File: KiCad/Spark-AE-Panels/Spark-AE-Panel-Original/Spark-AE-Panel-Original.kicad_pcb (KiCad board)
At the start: 4 copper layers, 50 x 101 mm, 1 part

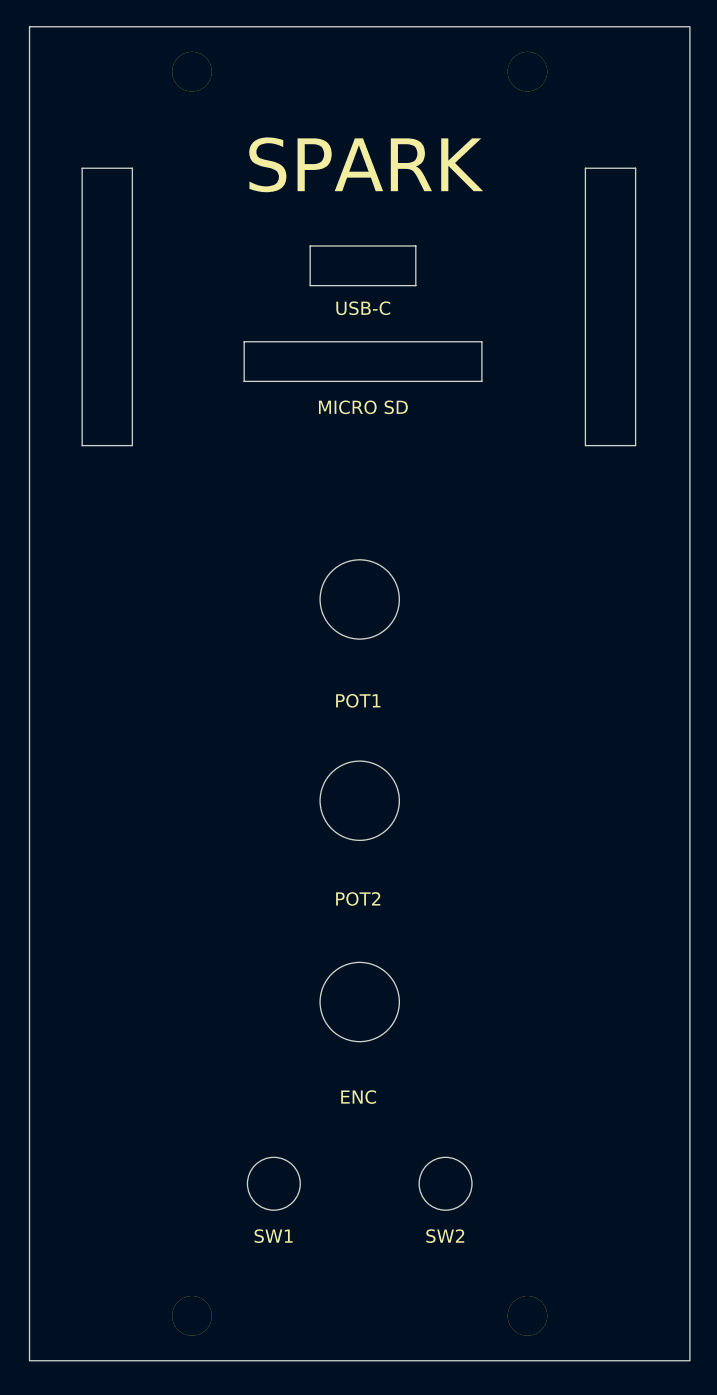
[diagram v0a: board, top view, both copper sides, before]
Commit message: rough pass over original mk0.1 panel. needs confirmation.
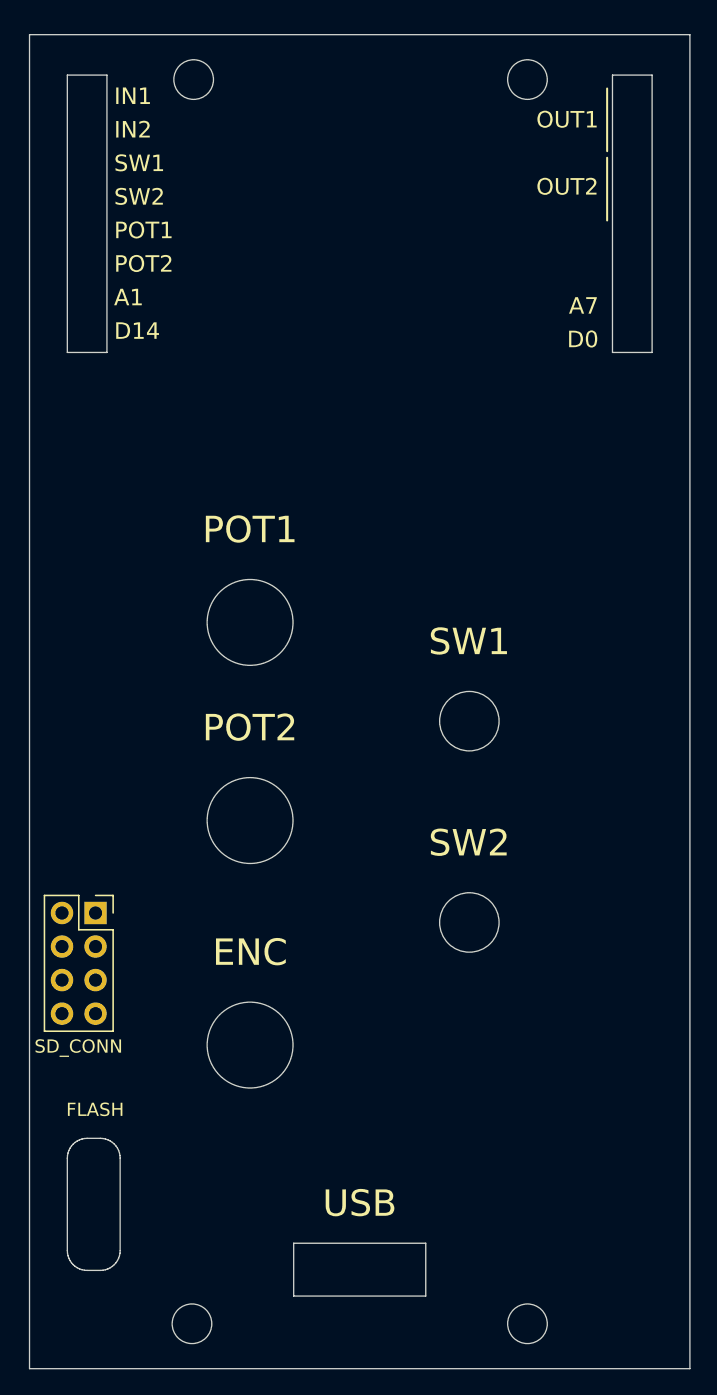
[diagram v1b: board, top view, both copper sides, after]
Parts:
- removed REF**: AE_2U_PANEL, clectric-diy:AE_2U_PANEL
- added J7: SD_CONN, Connector_PinSocket_2.54mm:PinSocket_2x04_P2.54mm_Vertical, F.Cu at (95.6, 112.3)
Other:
- outline, holes or cut-outs redrawn
- board text added: "A1"
- board text added: "A7"
- board text added: "D0"
- board text added: "D14"
- board text added: "FLASH"
- board text added: "IN1"
- board text added: "IN2"
- board text added: "OUT1"
- board text added: "OUT2"
- board text added: "USB"
- board text removed: "MICRO SD"
- board text removed: "SPARK"
- board text removed: "USB-C"

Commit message: removed front flash port. sorry.
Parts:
- removed J7: SD_CONN, Connector_PinSocket_2.54mm:PinSocket_2x04_P2.54mm_Vertical
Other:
- outline, holes or cut-outs redrawn
- board text removed: "FLASH"
